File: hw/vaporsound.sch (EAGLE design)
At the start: 75 parts, among them Q1 BSS138, Q2 BSS138

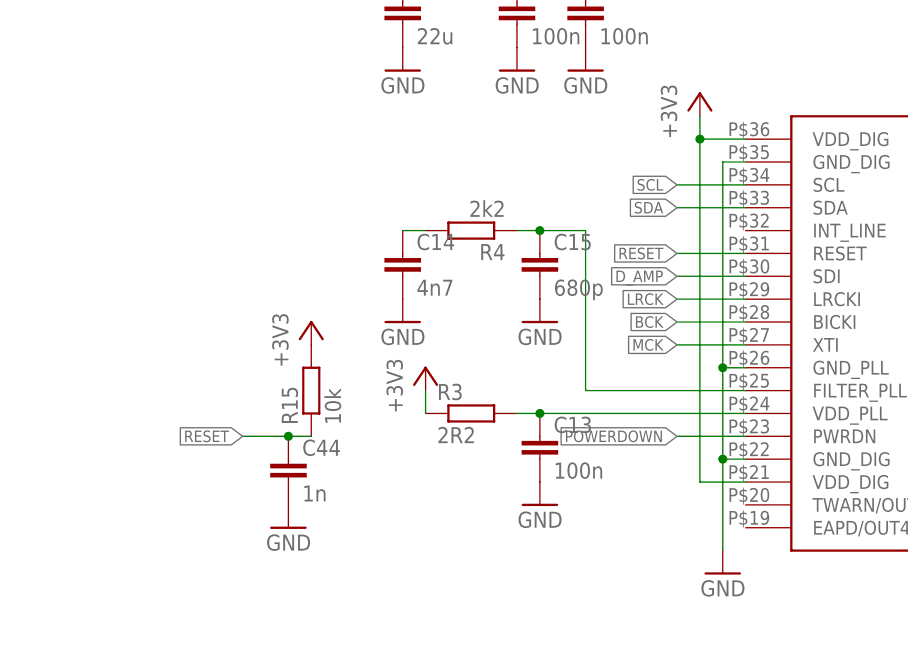
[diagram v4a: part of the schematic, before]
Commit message: begin component placement at input side of sta350
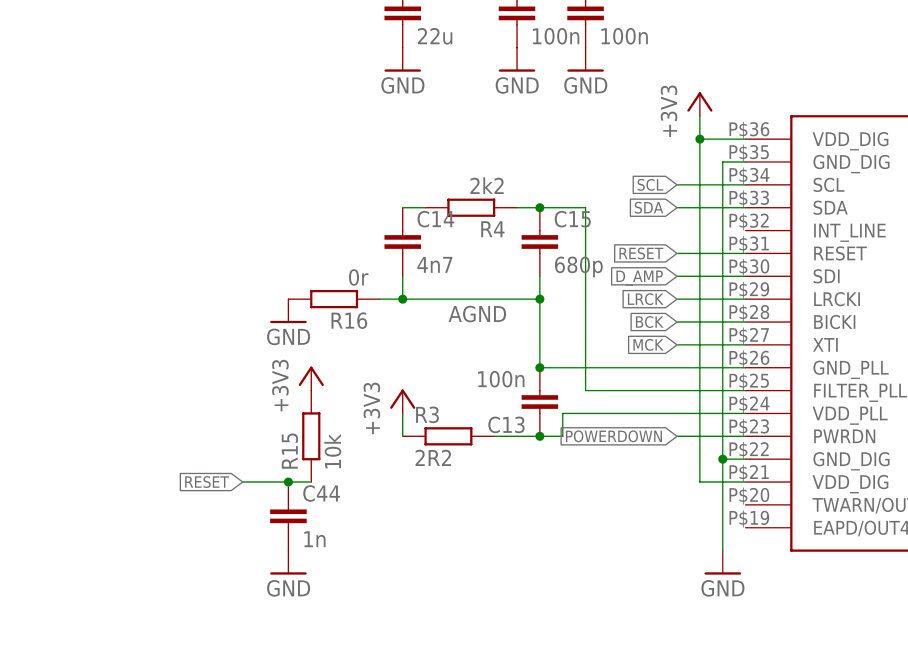
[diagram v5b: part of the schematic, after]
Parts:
- added R16: 0r, rcl:R-EU_R0603
- R3: device rcl:R-EU_R0805 -> rcl:R-EU_R0603
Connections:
- net N$1 renamed ADC_VREF
- net N$10 renamed FILTER_PLL
- net N$2 renamed C_RIGHT
- net N$22 renamed BOOST
- net N$24 renamed RIGHT_INPUT
- net N$29 renamed LEFT_INPUT
- net N$3 renamed VIN_R
- net N$4 renamed VIN_L
- net N$5 renamed C_LEFT
- new net AGND: C13.2, C14.2, C15.2, R16.1, U$1.GND_PLL
- net GND: now also R16.2; no longer C13.2, C14.2, C15.2, U$1.GND_PLL
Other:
- moved on the sheet: C13, C14, C15, C44, R15, R3, R4
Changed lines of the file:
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@@
 <part name="P+8" library="supply1" deviceset="+24V" device=""/>
 <part name="+3V2" library="supply1" deviceset="+3V3" device=""/>
-<part name="R3" library="rcl" deviceset="R-EU_" device="R0805" value="2R2"/>
+<part name="R3" library="rcl" deviceset="R-EU_" device="R0603" value="2R2"/>
 <part name="C13" library="rcl" deviceset="C-EU" device="C0402" value="100n"/>
-<part name="GND15" library="supply1" deviceset="GND" device=""/>
 <part name="C14" library="rcl" deviceset="C-EU" device="C0603" value="4n7"/>
 <part name="C15" library="rcl" deviceset="C-EU" device="C0603" value="680p"/>
 <part name="R4" library="rcl" deviceset="R-EU_" device="R0603" value="2k2"/>
-<part name="GND16" library="supply1" deviceset="GND" device=""/>
-<part name="GND17" library="supply1" deviceset="GND" device=""/>
 <part name="L1" library="srr1210-ind" deviceset="L-EU" device="SRR1210"/>
 <part name="L3" library="srr1210-ind" deviceset="L-EU" device="SRR1210"/>
@@
 <part name="+3V16" library="supply1" deviceset="+3V3" device=""/>
 <part name="GND43" library="supply1" deviceset="GND" device=""/>
+<part name="R16" library="rcl" deviceset="R-EU_" device="R0603" value="0r"/>
+<part name="GND16" library="supply1" deviceset="GND" device=""/>
 </parts>
 <sheets>
@@
 <instance part="C12" gate="G$1" x="248.92" y="60.96"/>
 <instance part="P+8" gate="1" x="248.92" y="48.26" rot="R270"/>
-<instance part="+3V2" gate="G$1" x="154.94" y="40.64"/>
-<instance part="R3" gate="G$1" x="160.02" y="35.56"/>
-<instance part="C13" gate="G$1" x="167.64" y="33.02"/>
-<instance part="GND15" gate="1" x="167.64" y="25.4" rot="MR0"/>
-<instance part="C14" gate="G$1" x="152.4" y="53.34"/>
-<instance part="C15" gate="G$1" x="167.64" y="53.34"/>
-<instance part="R4" gate="G$1" x="160.02" y="55.88" rot="R180"/>
-<instance part="GND16" gate="1" x="167.64" y="45.72" rot="MR0"/>
-<instance part="GND17" gate="1" x="152.4" y="45.72" rot="MR0"/>
+<instance part="+3V2" gate="G$1" x="152.4" y="38.1"/>
+<instance part="R3" gate="G$1" x="157.48" y="33.02"/>
+<instance part="C13" gate="G$1" x="167.64" y="35.56" rot="R180"/>
+<instance part="C14" gate="G$1" x="152.4" y="55.88"/>
+<instance part="C15" gate="G$1" x="167.64" y="55.88"/>
+<instance part="R4" gate="G$1" x="160.02" y="58.42" rot="R180"/>
 <instance part="L1" gate="G$1" x="279.4" y="17.78" rot="R90"/>
 <instance part="L3" gate="G$1" x="279.4" y="43.18" rot="R90"/>
@@
 <instance part="C42" gate="G$1" x="172.72" y="81.28"/>
 <instance part="C43" gate="G$1" x="165.1" y="81.28"/>
-<instance part="R15" gate="G$1" x="142.24" y="38.1" rot="R90"/>
-<instance part="+3V15" gate="G$1" x="142.24" y="45.72"/>
-<instance part="C44" gate="G$1" x="139.7" y="30.48"/>
-<instance part="GND40" gate="1" x="139.7" y="22.86" rot="MR0"/>
+<instance part="R15" gate="G$1" x="142.24" y="33.02" rot="R90"/>
+<instance part="+3V15" gate="G$1" x="142.24" y="40.64"/>
+<instance part="C44" gate="G$1" x="139.7" y="25.4"/>
+<instance part="GND40" gate="1" x="139.7" y="17.78" rot="MR0"/>
 <instance part="C45" gate="G$1" x="152.4" y="81.28"/>
 <instance part="+3V16" gate="G$1" x="152.4" y="86.36"/>
 <instance part="GND43" gate="1" x="152.4" y="73.66" rot="MR0"/>
+<instance part="R16" gate="G$1" x="144.78" y="48.26" rot="R180"/>
+<instance part="GND16" gate="1" x="139.7" y="45.72" rot="MR0"/>
 </instances>
 <busses>
@@
 <pinref part="GND6" gate="1" pin="GND"/>
 <wire x1="190.5" y1="63.5" x2="187.96" y2="63.5" width="0.1524" layer="91"/>
-<wire x1="187.96" y1="63.5" x2="187.96" y2="40.64" width="0.1524" layer="91"/>
-<pinref part="U$1" gate="G$1" pin="GND_PLL"/>
-<wire x1="187.96" y1="40.64" x2="187.96" y2="30.48" width="0.1524" layer="91"/>
+<wire x1="187.96" y1="63.5" x2="187.96" y2="30.48" width="0.1524" layer="91"/>
 <wire x1="187.96" y1="30.48" x2="187.96" y2="20.32" width="0.1524" layer="91"/>
-<wire x1="190.5" y1="40.64" x2="187.96" y2="40.64" width="0.1524" layer="91"/>
-<junction x="187.96" y="40.64"/>
 <pinref part="U$1" gate="G$1" pin="GND_DIG@1"/>
 <wire x1="190.5" y1="30.48" x2="187.96" y2="30.48" width="0.1524" layer="91"/>
 <junction x="187.96" y="30.48"/>
-</segment>
-<segment>
-<pinref part="C13" gate="G$1" pin="2"/>
-<pinref part="GND15" gate="1" pin="GND"/>
-</segment>
-<segment>
-<pinref part="C15" gate="G$1" pin="2"/>
-<pinref part="GND16" gate="1" pin="GND"/>
-</segment>
-<segment>
-<pinref part="C14" gate="G$1" pin="2"/>
-<pinref part="GND17" gate="1" pin="GND"/>
 </segment>
 <segment>
@@
 <pinref part="GND43" gate="1" pin="GND"/>
 </segment>
+<segment>
+<pinref part="R16" gate="G$1" pin="2"/>
+<pinref part="GND16" gate="1" pin="GND"/>
+</segment>
 </net>
 <net name="V+" class="0">
@@
 <pinref part="R3" gate="G$1" pin="1"/>
 <pinref part="+3V2" gate="G$1" pin="+3V3"/>
-<wire x1="154.94" y1="38.1" x2="154.94" y2="35.56" width="0.1524" layer="91"/>
+<wire x1="152.4" y1="35.56" x2="152.4" y2="33.02" width="0.1524" layer="91"/>
 </segment>
 <segment>
@@
 </segment>
 </net>
-<net name="N$1" class="0">
+<net name="ADC_VREF" class="0">
 <segment>
 <pinref part="U$3" gate="G$1" pin="VREF"/>
@@
 </segment>
 </net>
-<net name="N$2" class="0">
+<net name="C_RIGHT" class="0">
 <segment>
 <pinref part="R1" gate="G$1" pin="2"/>
@@
 </segment>
 </net>
-<net name="N$3" class="0">
+<net name="VIN_R" class="0">
 <segment>
 <pinref part="C9" gate="G$1" pin="1"/>
@@
 </segment>
 </net>
-<net name="N$4" class="0">
+<net name="VIN_L" class="0">
 <segment>
 <pinref part="C10" gate="G$1" pin="1"/>
@@
 </segment>
 </net>
-<net name="N$5" class="0">
+<net name="C_LEFT" class="0">
 <segment>
 <pinref part="R2" gate="G$1" pin="2"/>
@@
 </segment>
 <segment>
-<wire x1="134.62" y1="33.02" x2="139.7" y2="33.02" width="0.1524" layer="91"/>
-<label x="134.62" y="33.02" size="1.27" layer="95" rot="R180" xref="yes"/>
+<wire x1="134.62" y1="27.94" x2="139.7" y2="27.94" width="0.1524" layer="91"/>
+<label x="134.62" y="27.94" size="1.27" layer="95" rot="R180" xref="yes"/>
 <pinref part="R15" gate="G$1" pin="1"/>
 <pinref part="C44" gate="G$1" pin="1"/>
-<wire x1="139.7" y1="33.02" x2="142.24" y2="33.02" width="0.1524" layer="91"/>
-<junction x="139.7" y="33.02"/>
+<wire x1="139.7" y1="27.94" x2="142.24" y2="27.94" width="0.1524" layer="91"/>
+<junction x="139.7" y="27.94"/>
 </segment>
 </net>
@@
 <pinref part="R3" gate="G$1" pin="2"/>
 <pinref part="U$1" gate="G$1" pin="VDD_PLL"/>
-<wire x1="165.1" y1="35.56" x2="167.64" y2="35.56" width="0.1524" layer="91"/>
+<wire x1="162.56" y1="33.02" x2="167.64" y2="33.02" width="0.1524" layer="91"/>
 <pinref part="C13" gate="G$1" pin="1"/>
-<wire x1="167.64" y1="35.56" x2="190.5" y2="35.56" width="0.1524" layer="91"/>
-<junction x="167.64" y="35.56"/>
-</segment>
-</net>
-<net name="N$10" class="0">
+<wire x1="167.64" y1="33.02" x2="170.18" y2="33.02" width="0.1524" layer="91"/>
+<wire x1="170.18" y1="33.02" x2="170.18" y2="35.56" width="0.1524" layer="91"/>
+<wire x1="170.18" y1="35.56" x2="190.5" y2="35.56" width="0.1524" layer="91"/>
+<junction x="167.64" y="33.02"/>
+</segment>
+</net>
+<net name="FILTER_PLL" class="0">
 <segment>
 <pinref part="U$1" gate="G$1" pin="FILTER_PLL"/>
 <wire x1="190.5" y1="38.1" x2="172.72" y2="38.1" width="0.1524" layer="91"/>
-<wire x1="172.72" y1="38.1" x2="172.72" y2="55.88" width="0.1524" layer="91"/>
-<wire x1="172.72" y1="55.88" x2="167.64" y2="55.88" width="0.1524" layer="91"/>
+<wire x1="172.72" y1="38.1" x2="172.72" y2="58.42" width="0.1524" layer="91"/>
+<wire x1="172.72" y1="58.42" x2="167.64" y2="58.42" width="0.1524" layer="91"/>
 <pinref part="C15" gate="G$1" pin="1"/>
-<wire x1="167.64" y1="55.88" x2="165.1" y2="55.88" width="0.1524" layer="91"/>
-<junction x="167.64" y="55.88"/>
+<wire x1="167.64" y1="58.42" x2="165.1" y2="58.42" width="0.1524" layer="91"/>
+<junction x="167.64" y="58.42"/>
 <pinref part="R4" gate="G$1" pin="1"/>
 </segment>
@@
 <pinref part="R4" gate="G$1" pin="2"/>
 <pinref part="C14" gate="G$1" pin="1"/>
-<wire x1="152.4" y1="55.88" x2="154.94" y2="55.88" width="0.1524" layer="91"/>
+<wire x1="152.4" y1="58.42" x2="154.94" y2="58.42" width="0.1524" layer="91"/>
 </segment>
 </net>
@@
 </segment>
 </net>
-<net name="N$22" class="0">
+<net name="BOOST" class="0">
 <segment>
 <pinref part="U$2" gate="A" pin="BOOT@1"/>
@@
 </segment>
 </net>
-<net name="N$24" class="0">
+<net name="RIGHT_INPUT" class="0">
 <segment>
 <pinref part="C7" gate="G$1" pin="-"/>
@@
 </segment>
 </net>
-<net name="N$29" class="0">
+<net name="LEFT_INPUT" class="0">
 <segment>
 <pinref part="C8" gate="G$1" pin="-"/>
@@
 </segment>
 </net>
+<net name="AGND" class="0">
+<segment>
+<pinref part="U$1" gate="G$1" pin="GND_PLL"/>
+<pinref part="C15" gate="G$1" pin="2"/>
+<wire x1="190.5" y1="40.64" x2="167.64" y2="40.64" width="0.1524" layer="91"/>
+<wire x1="167.64" y1="40.64" x2="167.64" y2="48.26" width="0.1524" layer="91"/>
+<pinref part="C14" gate="G$1" pin="2"/>
+<wire x1="167.64" y1="48.26" x2="167.64" y2="50.8" width="0.1524" layer="91"/>
+<wire x1="152.4" y1="50.8" x2="152.4" y2="48.26" width="0.1524" layer="91"/>
+<wire x1="152.4" y1="48.26" x2="167.64" y2="48.26" width="0.1524" layer="91"/>
+<junction x="167.64" y="48.26"/>
+<pinref part="R16" gate="G$1" pin="1"/>
+<wire x1="149.86" y1="48.26" x2="152.4" y2="48.26" width="0.1524" layer="91"/>
+<junction x="152.4" y="48.26"/>
+<pinref part="C13" gate="G$1" pin="2"/>
+<junction x="167.64" y="40.64"/>
+<label x="157.48" y="45.72" size="1.778" layer="95"/>
+</segment>
+</net>

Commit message: use 0603 capacitors instead of 0402 ones
0603 is small enough for the board
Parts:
- C1, C13, C3, C42, C43, C5: device rcl:C-EUC0402 -> rcl:C-EUC0603
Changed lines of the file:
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@@
 <grid distance="0.1" unitdist="inch" unit="inch" style="lines" multiple="1" display="no" altdistance="0.01" altunitdist="inch" altunit="inch"/>
 <layers>
-<layer number="1" name="Top" color="4" fill="1" visible="no" active="no"/>
-<layer number="16" name="Bottom" color="1" fill="1" visible="no" active="no"/>
-<layer number="17" name="Pads" color="2" fill="1" visible="no" active="no"/>
-<layer number="18" name="Vias" color="2" fill="1" visible="no" active="no"/>
-<layer number="19" name="Unrouted" color="6" fill="1" visible="no" active="no"/>
-<layer number="20" name="Dimension" color="15" fill="1" visible="no" active="no"/>
-<layer number="21" name="tPlace" color="7" fill="1" visible="no" active="no"/>
-<layer number="22" name="bPlace" color="7" fill="1" visible="no" active="no"/>
-<layer number="23" name="tOrigins" color="15" fill="1" visible="no" active="no"/>
-<layer number="24" name="bOrigins" color="15" fill="1" visible="no" active="no"/>
-<layer number="25" name="tNames" color="7" fill="1" visible="no" active="no"/>
-<layer number="26" name="bNames" color="7" fill="1" visible="no" active="no"/>
-<layer number="27" name="tValues" color="7" fill="1" visible="no" active="no"/>
-<layer number="28" name="bValues" color="7" fill="1" visible="no" active="no"/>
+<layer number="1" name="Top" color="4" fill="1" visible="yes" active="no"/>
+<layer number="16" name="Bottom" color="1" fill="1" visible="yes" active="no"/>
+<layer number="17" name="Pads" color="2" fill="1" visible="yes" active="no"/>
+<layer number="18" name="Vias" color="2" fill="1" visible="yes" active="no"/>
+<layer number="19" name="Unrouted" color="6" fill="1" visible="yes" active="no"/>
+<layer number="20" name="Dimension" color="15" fill="1" visible="yes" active="no"/>
+<layer number="21" name="tPlace" color="7" fill="1" visible="yes" active="no"/>
+<layer number="22" name="bPlace" color="7" fill="1" visible="yes" active="no"/>
+<layer number="23" name="tOrigins" color="15" fill="1" visible="yes" active="no"/>
+<layer number="24" name="bOrigins" color="15" fill="1" visible="yes" active="no"/>
+<layer number="25" name="tNames" color="7" fill="1" visible="yes" active="no"/>
+<layer number="26" name="bNames" color="7" fill="1" visible="yes" active="no"/>
+<layer number="27" name="tValues" color="7" fill="1" visible="yes" active="no"/>
+<layer number="28" name="bValues" color="7" fill="1" visible="yes" active="no"/>
 <layer number="29" name="tStop" color="7" fill="3" visible="no" active="no"/>
 <layer number="30" name="bStop" color="7" fill="6" visible="no" active="no"/>
@@
 <layer number="35" name="tGlue" color="7" fill="4" visible="no" active="no"/>
 <layer number="36" name="bGlue" color="7" fill="5" visible="no" active="no"/>
-<layer number="37" name="tTest" color="7" fill="1" visible="no" active="no"/>
-<layer number="38" name="bTest" color="7" fill="1" visible="no" active="no"/>
+<layer number="37" name="tTest" color="7" fill="1" visible="yes" active="no"/>
+<layer number="38" name="bTest" color="7" fill="1" visible="yes" active="no"/>
 <layer number="39" name="tKeepout" color="4" fill="11" visible="no" active="no"/>
 <layer number="40" name="bKeepout" color="1" fill="11" visible="no" active="no"/>
@@
 <layer number="44" name="Drills" color="7" fill="1" visible="no" active="no"/>
 <layer number="45" name="Holes" color="7" fill="1" visible="no" active="no"/>
-<layer number="46" name="Milling" color="3" fill="1" visible="no" active="no"/>
-<layer number="47" name="Measures" color="7" fill="1" visible="no" active="no"/>
-<layer number="48" name="Document" color="7" fill="1" visible="no" active="no"/>
-<layer number="49" name="Reference" color="7" fill="1" visible="no" active="no"/>
-<layer number="50" name="dxf" color="7" fill="1" visible="no" active="no"/>
-<layer number="51" name="tDocu" color="7" fill="1" visible="no" active="no"/>
-<layer number="52" name="bDocu" color="7" fill="1" visible="no" active="no"/>
-<layer number="53" name="tGND_GNDA" color="7" fill="1" visible="no" active="no"/>
-<layer number="54" name="bGND_GNDA" color="7" fill="1" visible="no" active="no"/>
-<layer number="56" name="wert" color="7" fill="1" visible="no" active="no"/>
-<layer number="57" name="tCAD" color="7" fill="1" visible="no" active="no"/>
+<layer number="46" name="Milling" color="3" fill="1" visible="yes" active="no"/>
+<layer number="47" name="Measures" color="7" fill="1" visible="yes" active="no"/>
+<layer number="48" name="Document" color="7" fill="1" visible="yes" active="no"/>
+<layer number="49" name="Reference" color="7" fill="1" visible="yes" active="no"/>
+<layer number="50" name="dxf" color="7" fill="1" visible="yes" active="no"/>
+<layer number="51" name="tDocu" color="7" fill="1" visible="yes" active="no"/>
+<layer number="52" name="bDocu" color="7" fill="1" visible="yes" active="no"/>
+<layer number="53" name="tGND_GNDA" color="7" fill="1" visible="yes" active="no"/>
+<layer number="54" name="bGND_GNDA" color="7" fill="1" visible="yes" active="no"/>
+<layer number="56" name="wert" color="7" fill="1" visible="yes" active="no"/>
+<layer number="57" name="tCAD" color="7" fill="1" visible="yes" active="no"/>
 <layer number="90" name="Modules" color="5" fill="1" visible="yes" active="yes"/>
 <layer number="91" name="Nets" color="2" fill="1" visible="yes" active="yes"/>
@@
 <part name="P+5" library="supply1" deviceset="+5V" device=""/>
 <part name="+3V1" library="supply1" deviceset="+3V3" device=""/>
-<part name="C1" library="rcl" deviceset="C-EU" device="C0402" value="100n"/>
+<part name="C1" library="rcl" deviceset="C-EU" device="C0603" value="100n"/>
 <part name="C2" library="rcl" deviceset="C-EU" device="C0805"/>
 <part name="P+6" library="supply1" deviceset="V+" device=""/>
 <part name="GND7" library="supply1" deviceset="GND" device=""/>
 <part name="GND8" library="supply1" deviceset="GND" device=""/>
-<part name="C3" library="rcl" deviceset="C-EU" device="C0402" value="100n"/>
+<part name="C3" library="rcl" deviceset="C-EU" device="C0603" value="100n"/>
 <part name="C4" library="rcl" deviceset="C-EU" device="C0805"/>
 <part name="GND9" library="supply1" deviceset="GND" device=""/>
 <part name="GND10" library="supply1" deviceset="GND" device=""/>
-<part name="C5" library="rcl" deviceset="C-EU" device="C0402" value="100n"/>
+<part name="C5" library="rcl" deviceset="C-EU" device="C0603" value="100n"/>
 <part name="C6" library="rcl" deviceset="C-EU" device="C0805"/>
 <part name="GND11" library="supply1" deviceset="GND" device=""/>
@@
 <part name="+3V2" library="supply1" deviceset="+3V3" device=""/>
 <part name="R3" library="rcl" deviceset="R-EU_" device="R0603" value="2R2"/>
-<part name="C13" library="rcl" deviceset="C-EU" device="C0402" value="100n"/>
+<part name="C13" library="rcl" deviceset="C-EU" device="C0603" value="100n"/>
 <part name="C14" library="rcl" deviceset="C-EU" device="C0603" value="4n7"/>
 <part name="C15" library="rcl" deviceset="C-EU" device="C0603" value="680p"/>
@@
 <part name="+3V13" library="supply1" deviceset="+3V3" device=""/>
 <part name="+3V14" library="supply1" deviceset="+3V3" device=""/>
-<part name="C42" library="rcl" deviceset="C-EU" device="C0402" value="100n"/>
-<part name="C43" library="rcl" deviceset="C-EU" device="C0402" value="100n"/>
+<part name="C42" library="rcl" deviceset="C-EU" device="C0603" value="100n"/>
+<part name="C43" library="rcl" deviceset="C-EU" device="C0603" value="100n"/>
 <part name="R15" library="rcl" deviceset="R-EU_" device="R0603" value="10k"/>
 <part name="+3V15" library="supply1" deviceset="+3V3" device=""/>

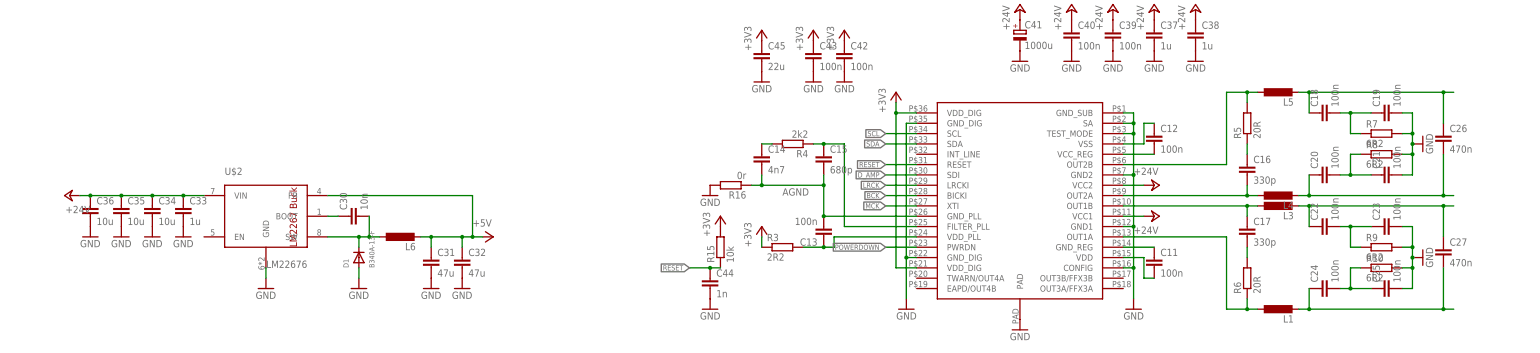
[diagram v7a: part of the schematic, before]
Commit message: output stage fully routed, adc routed
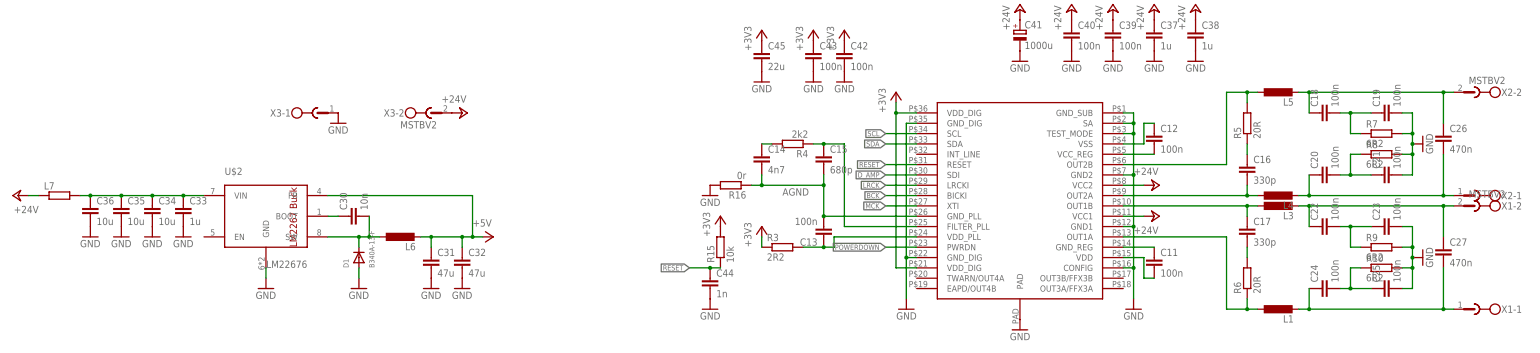
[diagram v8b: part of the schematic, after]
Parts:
- added L7: (no value), rcl:R-EU_R0805
- added X1, X2, X3: MSTBV2, con-phoenix-508:MSTBV2
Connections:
- new net 24V_DIGITAL: C33.1, C34.1, C35.1, C36.1, L7.2, U$2.VIN@7
- net +24V: now also L7.1, X3-2.1; no longer C33.1, C34.1, C35.1, C36.1, U$2.VIN@7
- net GND: now also X3-1.1
- net SPKR1A: now also X1-1.1
- net SPKR1B: now also X1-2.1
- net SPKR2A: now also X2-1.1
- net SPKR2B: now also X2-2.1
